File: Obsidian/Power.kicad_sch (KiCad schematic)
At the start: 80 parts, among them J10 Barrel_Jack_Switch, J16 Conn_01x04, Q4 DMP3013SFV, U10 TPSM863257RDXR, U11 TPSM863257RDXR, U18 TLV77325PDBVR, U20 RT9045AGSP / AP2303, U23 LD39100PU12RY, U24 SN74LVC1G07DBV, U25 SN74LVC1G07DBV, U4 TPSM863257RDXR, U5 TPSM863257RDXR, U6 TPSM863257RDXR

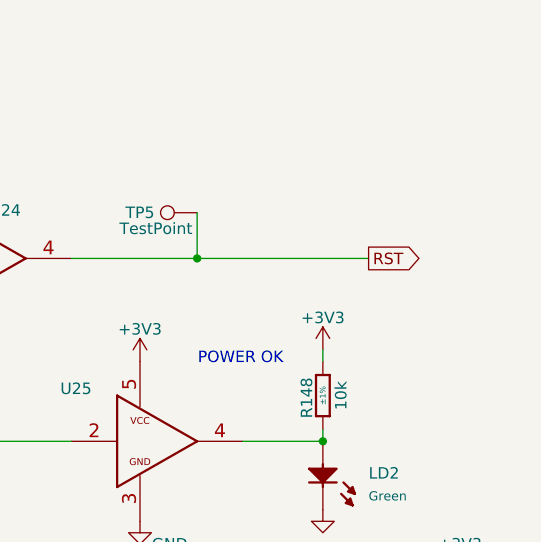
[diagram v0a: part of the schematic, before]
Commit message: removing reset global label
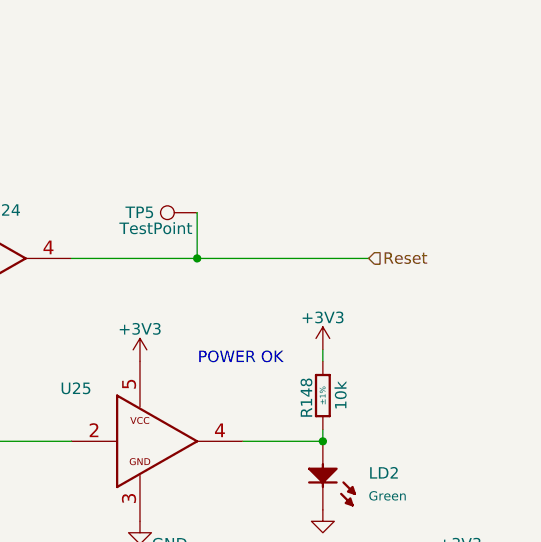
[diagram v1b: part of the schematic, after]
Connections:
- net RST renamed Reset
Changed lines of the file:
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@@
 		)
 	)
-	(global_label "RST"
-		(shape output)
+	(hierarchical_label "Reset"
+		(shape input)
 		(at 254 36.83 0)
-		(fields_autoplaced yes)
 		(effects
 			(font
@@
 			(justify left)
 		)
-		(property "Intersheetrefs" "${INTERSHEET_REFS}"
-			(at 260.4323 36.83 0)
-			(effects
-				(font
-					(size 1.27 1.27)
-				)
-				(justify left)
-				(hide yes)
-			)
-		)
 	)

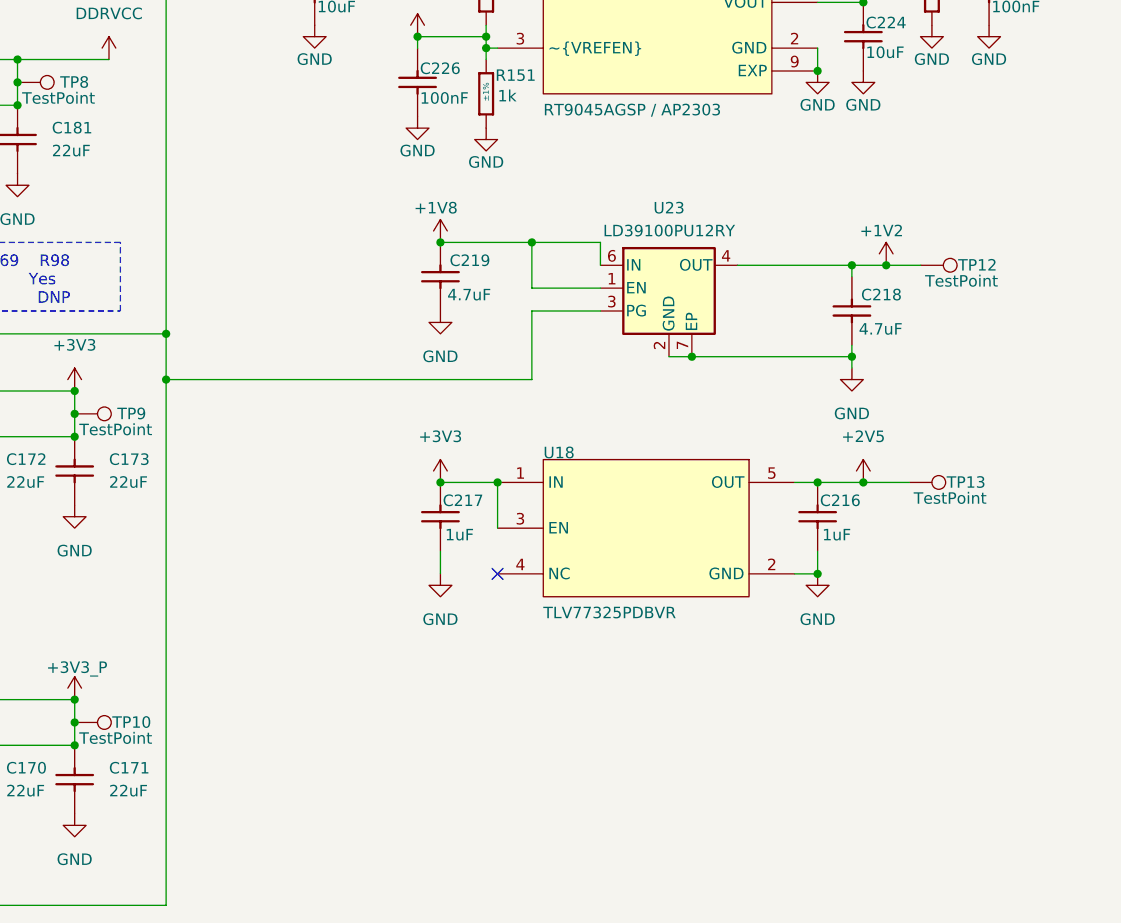
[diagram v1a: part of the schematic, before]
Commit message: adding 1V regulator for MGT transceiver
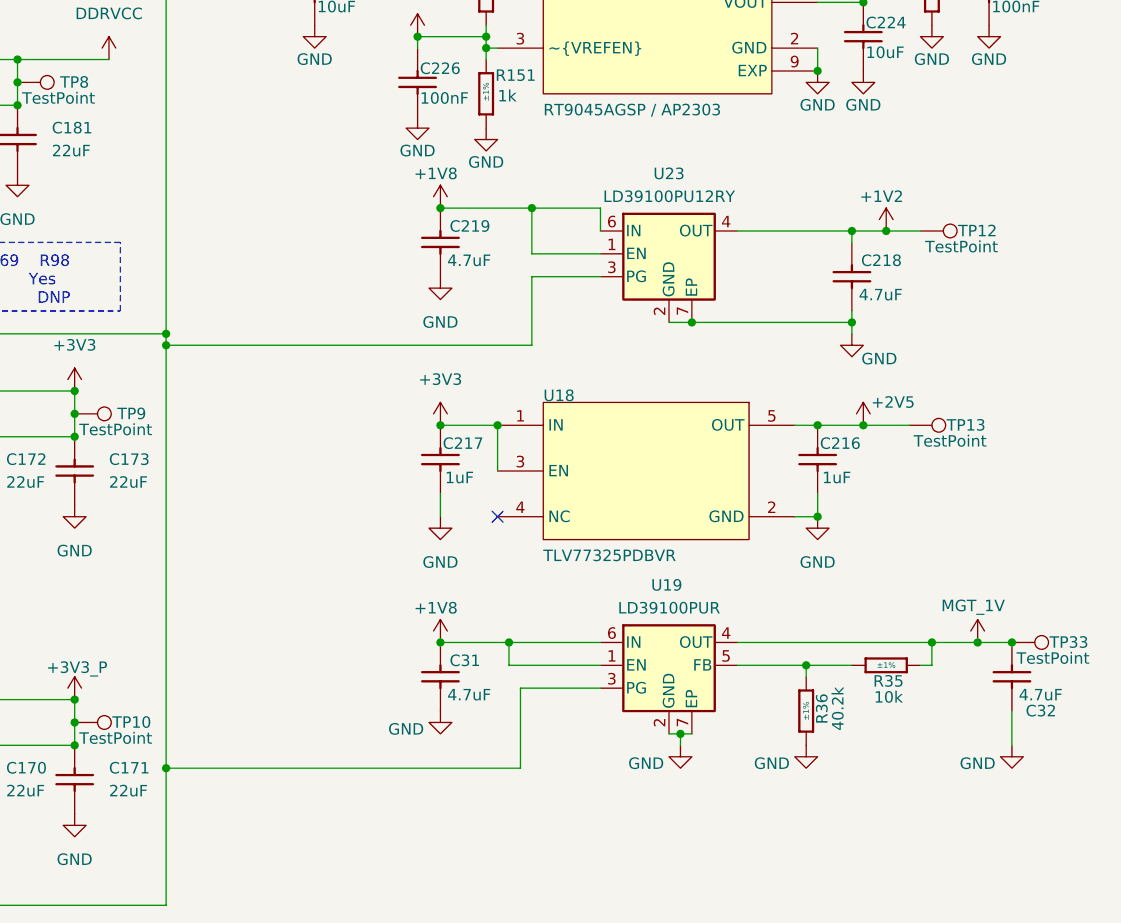
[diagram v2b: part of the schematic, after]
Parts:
- added C31, C32: CC0402_4.7UF_16V_20%_X5R, Capacitor_SMD:C_0402_1005Metric, symbol Library_Symbol:CC0402_4.7UF_16V_20%_X5R
- added R35: R0402_10K_1%_0.0625W_100PPM, Footprint:RESC1005X40N, symbol Library_Symbol:R0402_10K_1%_0.0625W_100PPM
- added R36: R0402_40.2K_1%_0.0625W_100PPM, Footprint:RESC1005X40N, symbol Library_Symbol:R0402_10K_1%_0.0625W_100PPM
- added TP33: TestPoint, TestPoint:TestPoint_Pad_D1.5mm, symbol Library_Symbol:TestPoint
- added U19: LD39100PUR, Package_DFN_QFN:DFN-6-1EP_3x3mm_P0.95mm_EP1.7x2.6mm, symbol Library_Symbol:LD39100PUR_DFN6
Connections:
- net +1V8: now also C31.2, U19.1 (EN), U19.6 (IN)
- net GND: now also C31.1, C32.1, R36.2, U19.2 (GND), U19.7 (EP)
- net at D3.1 (K), LD1.1 (C), TP6.1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: now also U19.3 (PG)
- new net: R35.2, R36.1, U19.5 (FB)
- new net MGT_1V: C32.2, R35.1, TP33.1, U19.4 (OUT)
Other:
- moved on the sheet: C216, C217, C218, C219, TP12, TP13, U18, U23

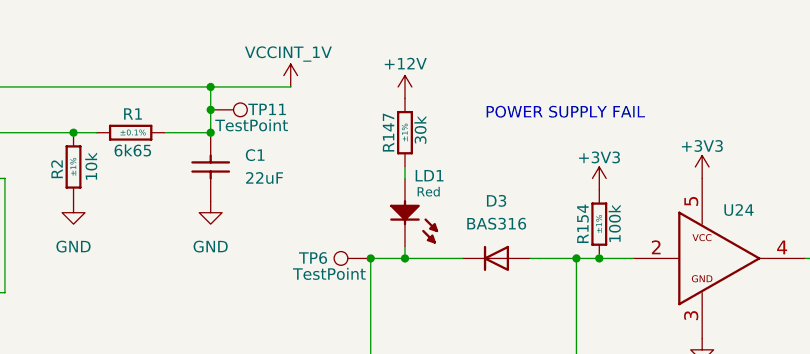
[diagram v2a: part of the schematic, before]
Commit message: Modifying line voltage for certain components, adding pull up resistor
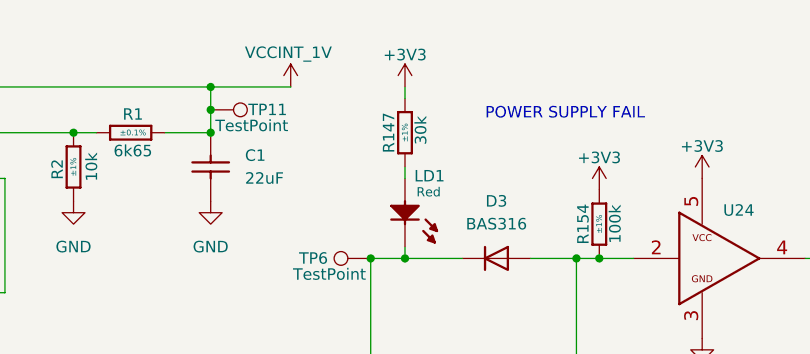
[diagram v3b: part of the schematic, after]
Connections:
- net +12V: no longer R147.1
- net +3V3: now also R147.1
- net at U19.5 (FB): now also R35.2, R36.1
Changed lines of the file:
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@@
 		)
 	)
+	(wire
+		(pts
+			(xy 176.53 17.78) (xy 176.53 19.05)
+		)
+		(stroke
+			(width 0)
+			(type default)
+		)
+	)
 	(polyline
 		(pts
@@
 		(pin "7"
 		)
-		(pin "5"
-		)
 		(instances
 			(project "Obsidian"
@@
 	)
 	(symbol
+		(lib_id "Library_Symbol:+1V0")
+		(at 176.53 17.78 0)
+		(unit 1)
+		(exclude_from_sim no)
+		(in_bom yes)
+		(on_board yes)
+		(dnp no)
+		(property "Reference" "#PWR062"
+			(at 176.53 21.59 0)
+			(effects
+				(font
+					(size 1.27 1.27)
+				)
+				(hide yes)
+			)
+		)
+		(property "Value" "+3V3"
+			(at 176.53 14.224 0)
+			(effects
+				(font
+					(size 1.27 1.27)
+				)
+			)
+		)
+		(property "Footprint" ""
+			(at 176.53 17.78 0)
+			(effects
+				(font
+					(size 1.27 1.27)
+				)
+				(hide yes)
+			)
+		)
+		(property "Datasheet" ""
+			(at 176.53 17.78 0)
+			(effects
+				(font
+					(size 1.27 1.27)
+				)
+				(hide yes)
+			)
+		)
+		(property "Description" "Power symbol creates a global label with name \"+1V0\""
+			(at 176.53 17.78 0)
+			(effects
+				(font
+					(size 1.27 1.27)
+				)
+				(hide yes)
+			)
+		)
+		(pin "1"
+		)
+		(instances
+			(project "Obsidian"
+				(path "/c2a4f786-b14c-434a-acf7-b20fb2221b0b/1f98e56a-3346-4f12-a356-5cd64c4ccde0"
+					(reference "#PWR062")
+					(unit 1)
+				)
+			)
+		)
+	)
+	(symbol
 		(lib_id "Library_Symbol:GND")
 		(at 139.7 97.79 0)
@@
 					(unit 1)
 				)
-			)
-		)
-	)
-	(symbol
-		(lib_id "Library_Symbol:+12V")
-		(at 176.53 19.05 0)
-		(unit 1)
-		(exclude_from_sim no)
-		(in_bom yes)
-		(on_board yes)
-		(dnp no)
-		(property "Reference" "#PWR0297"
-			(at 176.53 22.86 0)
-			(effects
-				(font
-					(size 1.27 1.27)
-				)
-				(hide yes)
-			)
-		)
-		(property "Value" "+12V"
-			(at 176.53 15.24 0)
-			(effects
-				(font
-					(size 1.27 1.27)
-				)
-			)
-		)
-		(property "Footprint" ""
-			(at 176.53 19.05 0)
-			(effects
-				(font
-					(size 1.27 1.27)
-				)
-				(hide yes)
-			)
-		)
-		(property "Datasheet" ""
-			(at 176.53 19.05 0)
-			(effects
-				(font
-					(size 1.27 1.27)
-				)
-				(hide yes)
-			)
-		)
-		(property "Description" "Power symbol creates a global label with name \"+12V\""
-			(at 176.53 19.05 0)
-			(effects
-				(font
-					(size 1.27 1.27)
-				)
-				(hide yes)
-			)
-		)
-		(pin "1"
-		)
-		(instances
-			(project "Marble_Tiny"
-				(path "/c2a4f786-b14c-434a-acf7-b20fb2221b0b/1f98e56a-3346-4f12-a356-5cd64c4ccde0"
-					(reference "#PWR0297")
-					(unit 1)
-				)

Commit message: update LCSC reference, and OFFSET rotation for JLCPCB
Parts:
- C218, C219, C225, C226, C228, C31, C32: footprint Capacitor_SMD:C_0402_1005Metric -> Footprint:CAPC1005X55N
- LD2: LCSC C5879295 -> C598257
- R91, R94: LCSC (none) -> C861113
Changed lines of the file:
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@@
 			)
 		)
-		(property "LCSC" ""
+		(property "LCSC" "C861113"
 			(at 147.32 161.29 0)
 			(effects
@@
 			)
 		)
-		(property "Footprint" "Capacitor_SMD:C_0402_1005Metric"
+		(property "Footprint" "Footprint:CAPC1005X55N"
 			(at 70.358 25.4 0)
 			(effects
@@
 			)
 		)
-		(property "Footprint" "Capacitor_SMD:C_0402_1005Metric"
+		(property "Footprint" "Footprint:CAPC1005X55N"
 			(at 211.328 109.22 0)
 			(effects
@@
 			)
 		)
-		(property "Footprint" "Capacitor_SMD:C_0402_1005Metric"
+		(property "Footprint" "Footprint:CAPC1005X55N"
 			(at 208.788 91.44 0)
 			(effects
@@
 			)
 		)
-		(property "Footprint" "Capacitor_SMD:C_0402_1005Metric"
+		(property "Footprint" "Footprint:CAPC1005X55N"
 			(at 257.048 113.03 0)
 			(effects
@@
 			)
 		)
-		(property "Footprint" "Capacitor_SMD:C_0402_1005Metric"
+		(property "Footprint" "Footprint:CAPC1005X55N"
 			(at 274.828 157.48 0)
 			(effects
@@
 			)
 		)
-		(property "LCSC" "C5879295"
+		(property "LCSC" "C598257"
 			(at 248.92 60.96 90)
 			(effects
@@
 			)
 		)
-		(property "Footprint" "Capacitor_SMD:C_0402_1005Metric"
+		(property "Footprint" "Footprint:CAPC1005X55N"
 			(at 272.288 81.28 0)
 			(effects
@@
 			)
 		)
-		(property "LCSC" ""
+		(property "LCSC" "C861113"
 			(at 147.32 127 0)
 			(effects
@@
 			)
 		)
-		(property "Footprint" "Capacitor_SMD:C_0402_1005Metric"
+		(property "Footprint" "Footprint:CAPC1005X55N"
 			(at 211.328 157.48 0)
 			(effects

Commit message: adding production files, and documentations
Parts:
- J16: LCSC (none) -> C3309598
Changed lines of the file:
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@@
+			)
+		)
+		(property "LCSC" "C3309598"
+			(at 19.05 43.18 0)
+			(effects
+				(font
+					(size 1.27 1.27)
+				)
+				(hide yes)
 			)
 		)

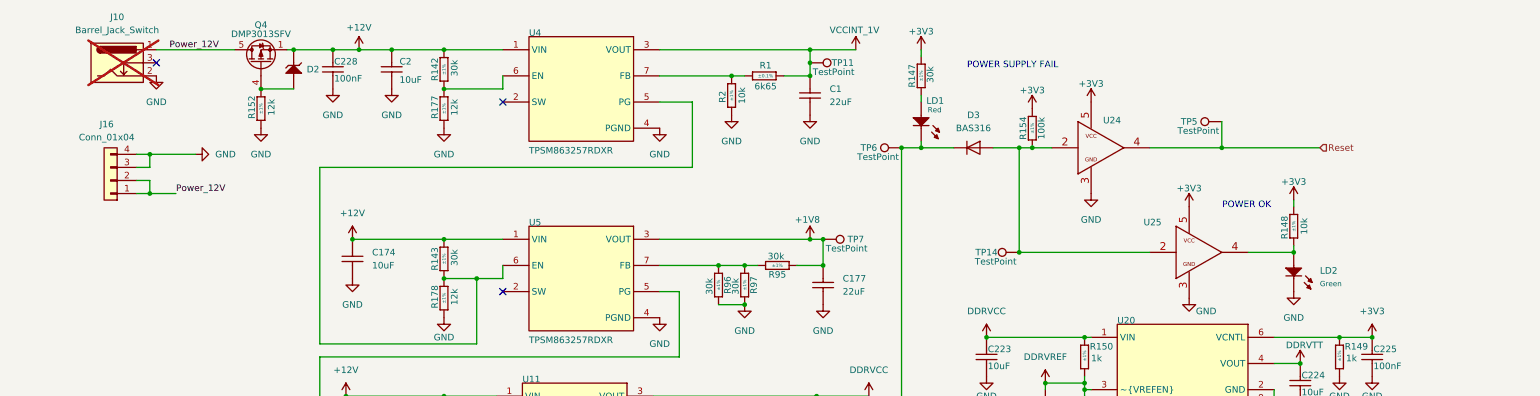
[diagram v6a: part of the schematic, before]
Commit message: Adding documentation for configuration with flash memory, adding more comments to schematic
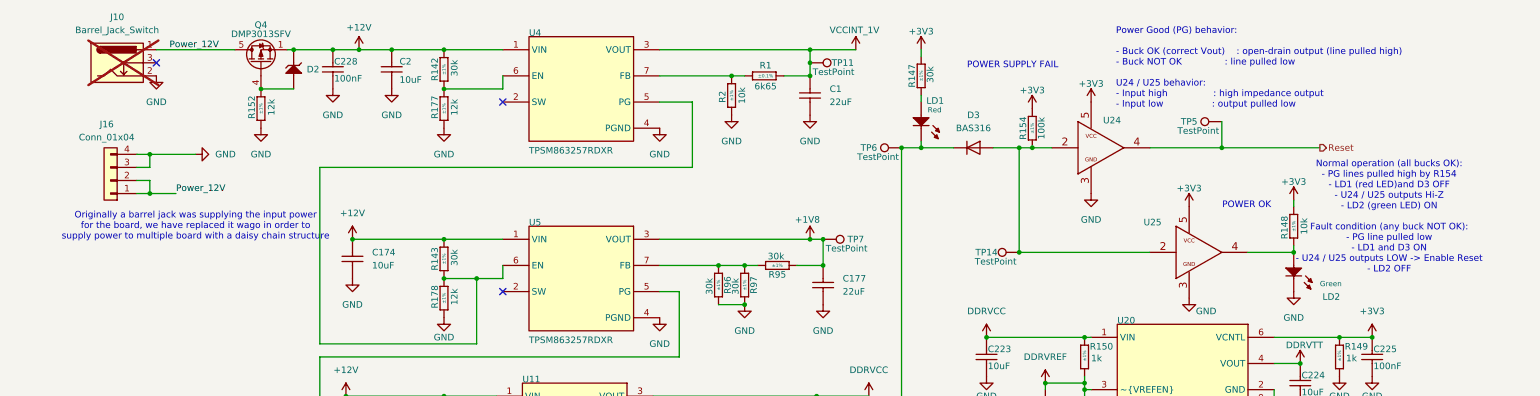
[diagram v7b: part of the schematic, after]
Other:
- note added: "Normal operation (all bucks OK): - PG lines pulled high by R154 - LD1 (red LED)and D3 OFF - U24 / U25 outputs Hi-Z - LD2 (green LED) ON Fault condition (any buck NOT OK): - PG line pulled low - LD1 and D3 ON - U24 / U25 outputs LOW -> Enable Reset - LD2 OFF"
- note added: "Originally a barrel jack was supplying the input power for the board, we have replaced it wago in order to supply power to multiple board with a daisy chain structure"
- note added: "Power Good (PG) behavior: - Buck OK (correct Vout) : open-drain output (line pulled high) - Buck NOT OK : line pulled low U24 / U25 behavior: - Input high : high impedance output - Input low : output pulled low"
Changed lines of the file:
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@@
 		)
 	)
+	(text "Normal operation (all bucks OK):\n- PG lines pulled high by R154\n- LD1 (red LED)and D3 OFF\n- U24 / U25 outputs Hi-Z\n- LD2 (green LED) ON\n\nFault condition (any buck NOT OK):\n- PG line pulled low\n- LD1 and D3 ON\n- U24 / U25 outputs LOW -> Enable Reset\n- LD2 OFF"
+		(exclude_from_sim no)
+		(at 267.462 50.292 0)
+		(effects
+			(font
+				(face "Arial")
+				(size 1.27 1.27)
+			)
+		)
+	)
 	(text "POWER OK"
 		(exclude_from_sim no)
@@
 		)
 	)
+	(text "Power Good (PG) behavior:\n\n- Buck OK (correct Vout)    : open-drain output (line pulled high)\n- Buck NOT OK               : line pulled low\n\nU24 / U25 behavior:\n- Input high                : high impedance output\n- Input low                 : output pulled low"
+		(exclude_from_sim no)
+		(at 214.376 21.336 0)
+		(effects
+			(font
+				(size 1.27 1.27)
+			)
+			(justify left)
+		)
+	)
+	(text "Originally a barrel jack was supplying the input power\nfor the board, we have replaced it wago in order to\nsupply power to multiple board with a daisy chain structure "
+		(exclude_from_sim no)
+		(at 35.56 52.07 0)
+		(effects
+			(font
+				(size 1.27 1.27)
+			)
+		)
+	)
 	(junction
 		(at 139.7 22.86)
@@
 	)
 	(hierarchical_label "Reset"
-		(shape input)
+		(shape output)
 		(at 254 36.83 0)
 		(effects
@@
 		(on_board yes)
 		(dnp no)
-		(fields_autoplaced yes)
 		(property "Reference" "LD2"
-			(at 254 60.7059 90)
+			(at 254.508 65.786 90)
 			(effects
 				(font
